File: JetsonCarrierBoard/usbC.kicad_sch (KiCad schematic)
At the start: 28 parts, among them J4 USB_C_Receptacle, U5 TPS65987D, U6 TPD6S300A, U7 HD3SS460

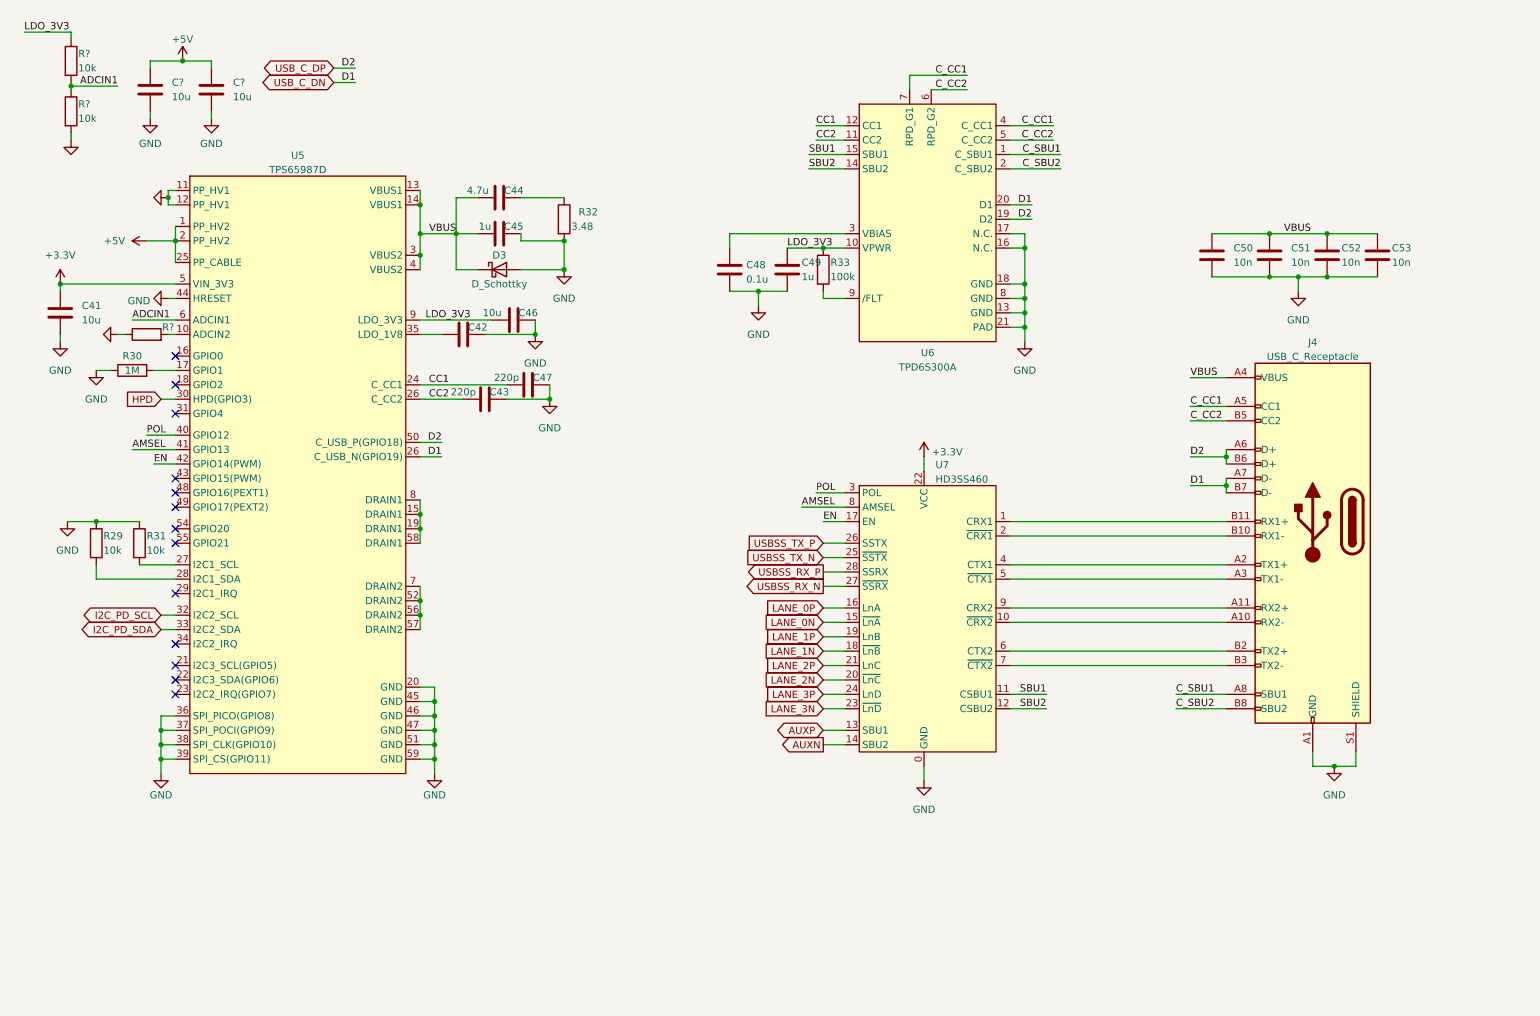
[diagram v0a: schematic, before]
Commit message: Organize and Fix USB-C Part
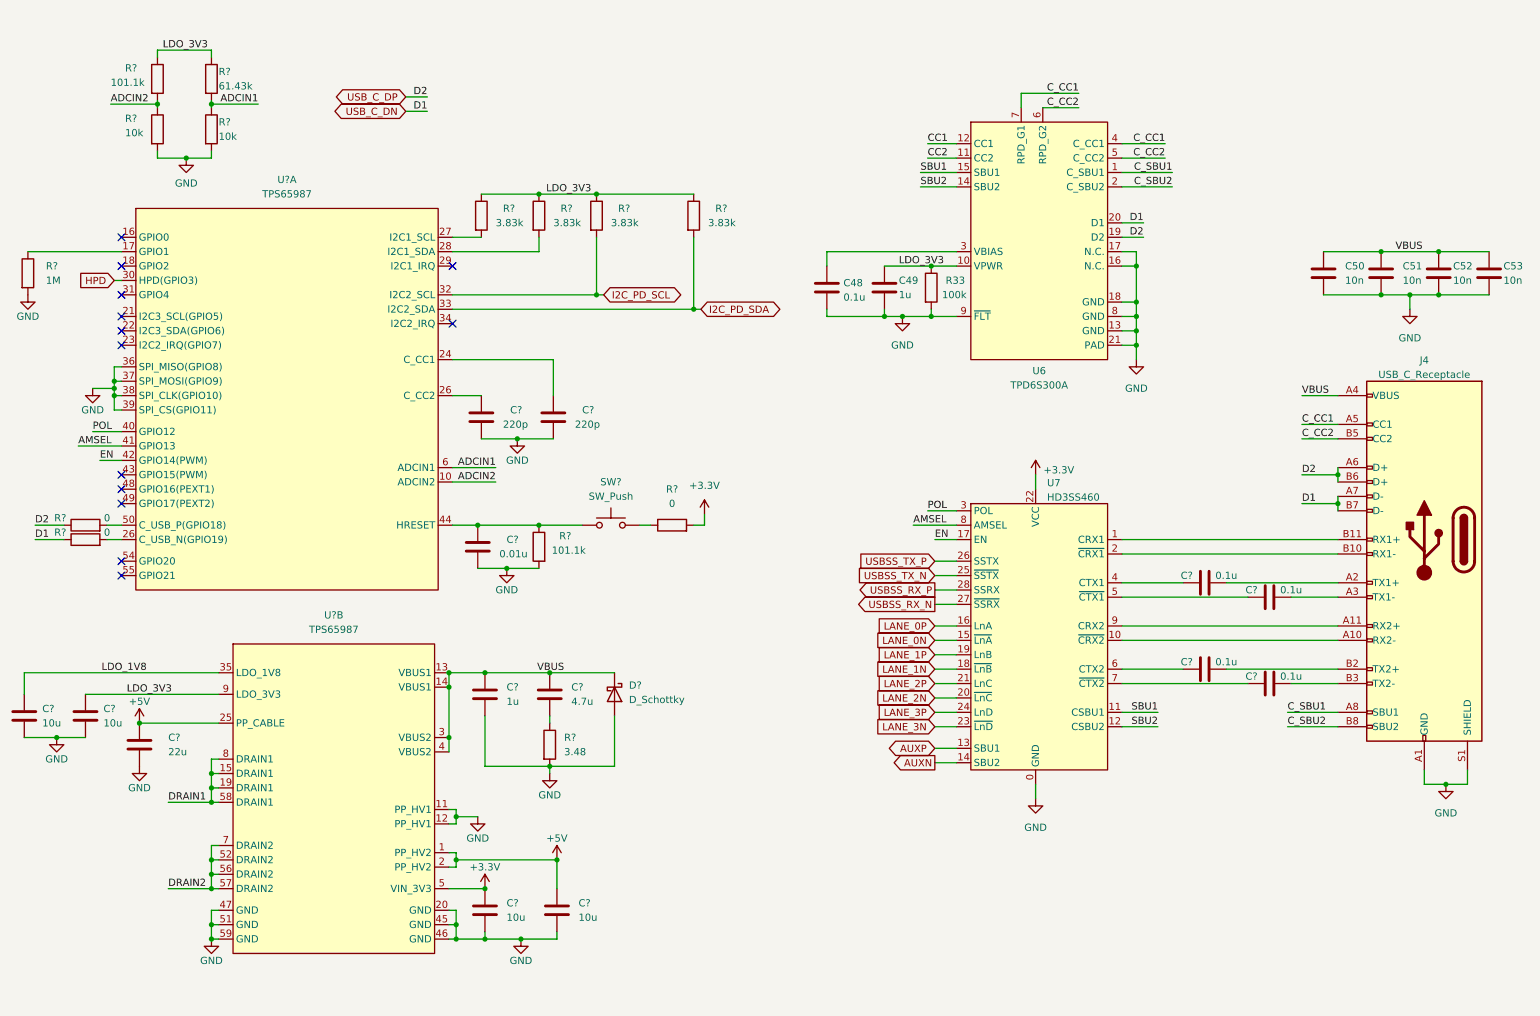
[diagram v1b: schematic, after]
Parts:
- removed C41, C46, C? (x2): 10u, symbol Device:C
- removed C42: (no value), symbol Device:C
- removed C43, C47: 220p, symbol Device:C
- removed C44: 4.7u, symbol Device:C
- removed C45: 1u, symbol Device:C
- removed D3: D_Schottky, symbol Device:D_Schottky
- removed R29, R31: 10k, symbol Device:R
- removed R30: 1M, symbol Device:R
- removed R32: 3.48, symbol Device:R
- removed R?: (no value), symbol Device:R
- removed U5: TPS65987D, symbol PD_controller:TPS65987D
- added C?: 1u, symbol Device:C
- added C? (x4): 10u, symbol Device:C
- added C?: 22u, symbol Device:C
- added C? (x4): 0.1u, symbol Device:C
- added C? (x2): 220p, symbol Device:C
- added C?: 4.7u, symbol Device:C
- added C?: 0.01u, symbol Device:C
- added D?: D_Schottky, symbol Device:D_Schottky
- added R? (x4): 3.83k, symbol Device:R
- added R? (x3): 0, symbol Device:R
- added R?: 3.48, symbol Device:R
- added R? (x2): 101.1k, symbol Device:R
- added R?: 10k, symbol Device:R
- added R?: 1M, symbol Device:R
- added SW?: SW_Push, symbol Switch:SW_Push
- added U? (x2): TPS65987, symbol PD_controller:TPS65987
- R?: value 10k -> 61.43k
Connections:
- net +3.3V: now also C?.2, R?.2, U?.5 (VIN_3V3)
- net +5V: now also C?.2, C?.2, U?.1 (PP_HV2), U?.2 (PP_HV2), U?.25 (PP_CABLE)
- net ADCIN1: now also U?.6 (ADCIN1)
- net AMSEL: now also U?.41 (GPIO13)
- net EN: now also U?.42 (GPIO14(PWM))
- net GND: now also R33.2, U6.9 (~{FLT}), C?.1, C?.1, C?.1, C?.1, C?.1, C?.1, C?.1, C?.1, C?.1, D?.2 (A), R?.2, R?.2, R?.2, R?.2, U?.11 (PP_HV1), U?.12 (PP_HV1), U?.20 (GND), U?.36 (SPI_MISO(GPIO8)), U?.37 (SPI_MOSI(GPIO9)), U?.38 (SPI_CLK(GPIO10)), U?.39 (SPI_CS(GPIO11)), U?.45 (GND), U?.46 (GND), U?.47 (GND), U?.51 (GND), U?.59 (GND)
- net HPD: now also U?.30 (HPD(GPIO3))
- net I2C_PD_SCL: now also R?.2, U?.32 (I2C2_SCL)
- net I2C_PD_SDA: now also R?.2, U?.33 (I2C2_SDA)
- net LDO_3V3: now also C?.2, R?.1, R?.1, R?.1, R?.1, R?.1, U?.9 (LDO_3V3)
- net POL: now also U?.40 (GPIO12)
- net USB_C_DN: now also R?.1
- net USB_C_DP: now also R?.1
- net VBUS: now also C?.2, C?.2, D?.1 (K), U?.13 (VBUS1), U?.14 (VBUS1), U?.3 (VBUS2), U?.4 (VBUS2)
- net at J4.A2 (TX1+): now also C?.2; no longer U7.4 (CTX1)
- net at J4.A3 (TX1-): now also C?.2; no longer U7.5 (~{CTX1})
- net at U7.6 (CTX2): now also C?.1; no longer J4.B2 (TX2+)
- net at J4.B3 (TX2-): now also C?.2; no longer U7.7 (~{CTX2})
- new net: R?.2, U?.28 (I2C1_SDA)
- new net: C?.2, J4.B2 (TX2+)
- new net: R?.2, U?.50 (C_USB_P(GPIO18))
- new net: R?.1, SW?.2
- new net: C?.1, R?.1
- new net: C?.2, U?.26 (C_USB_N(GPIO19))
- new net: C?.1, U7.4 (CTX1)
- new net: C?.1, U7.5 (~{CTX1})
- new net: C?.2, R?.1, SW?.1, U?.44 (HRESET)
- new net: C?.1, U7.7 (~{CTX2})
- new net: R?.1, U?.17 (GPIO1)
- new net: C?.2, U?.24 (C_CC1)
- new net: R?.2, U?.26 (C_USB_N(GPIO19))
- new net: R?.2, U?.27 (I2C1_SCL)
- new net ADCIN2: R?.1, R?.2, U?.10 (ADCIN2)
- new net DRAIN1: U?.15 (DRAIN1), U?.19 (DRAIN1), U?.58 (DRAIN1), U?.8 (DRAIN1)
- new net DRAIN2: U?.52 (DRAIN2), U?.56 (DRAIN2), U?.57 (DRAIN2), U?.7 (DRAIN2)
- new net LDO_1V8: C?.2, U?.35 (LDO_1V8)
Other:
- moved on the sheet: C48, C49, C50, C51, C52, C53, J4, R33, R?, U6, U7

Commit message: USB-C Changes
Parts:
- removed C?: 4.7u, symbol Device:C
- removed D?: D_Schottky, symbol Device:D_Schottky
- removed R?: 3.48, symbol Device:R
- added C?: 4.7u, symbol Device:C
- added C?: 0.1u, symbol Device:C
- added D?: D, symbol Device:D_Schottky
- added R? (x4): 3.3k, symbol Device:R
- added R?: 3.48, symbol Device:R
- added U?: W25Q80, Package_SO:SOIC-8_5.23x5.23mm_P1.27mm, symbol Memory_Flash:W25Q128JVS
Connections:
- net GND: now also D?.2 (A), R?.2, U?.4 (GND); no longer U?.36 (SPI_MISO(GPIO8)), U?.37 (SPI_MOSI(GPIO9)), U?.38 (SPI_CLK(GPIO10)), U?.39 (SPI_CS(GPIO11))
- net VBUS: now also C?.2, D?.1 (K)
- new net: C?.2, R?.1, R?.1, R?.1, R?.1, U?.8 (VCC)
- new net: C?.1, R?.1
- new net: R?.2, U?.3 (IO2)
- new net: R?.2, U?.7 (IO3)
- new net CS: C?.1, R?.2, U?.1 (~{CS}), U?.39 (SPI_CS(GPIO11))
- new net MISO: R?.2, U?.2 (DO(IO1)), U?.36 (SPI_MISO(GPIO8))
- new net MOSI: U?.37 (SPI_MOSI(GPIO9)), U?.5 (DI(IO0))
- new net SCLK: U?.38 (SPI_CLK(GPIO10)), U?.6 (CLK)
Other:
- moved on the sheet: C48, C49, C50, C51, C52, C53, C?, J4, R33, U6, U7, U?B
